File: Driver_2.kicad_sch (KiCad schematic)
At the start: 36 parts

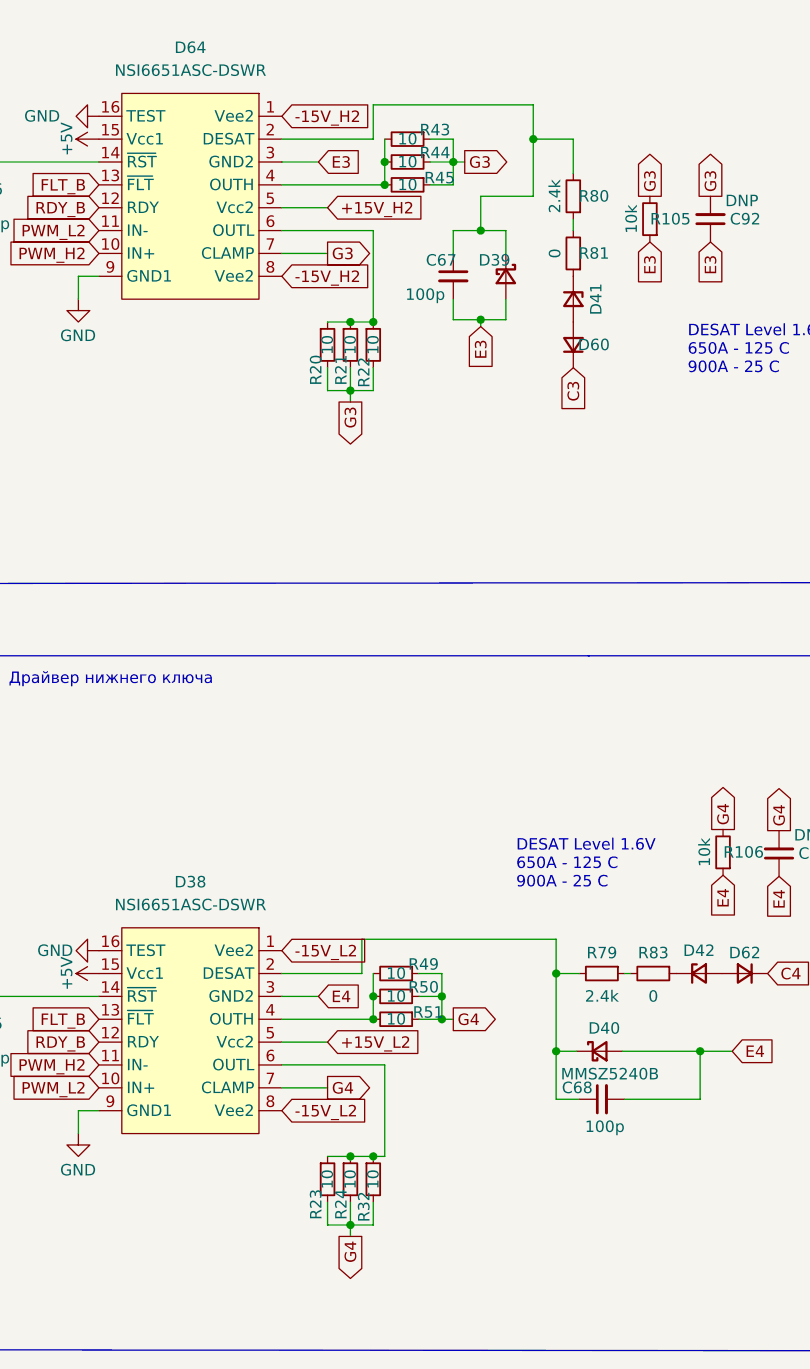
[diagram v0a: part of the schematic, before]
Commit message: VER2.2: удалил лишний затворный резистор
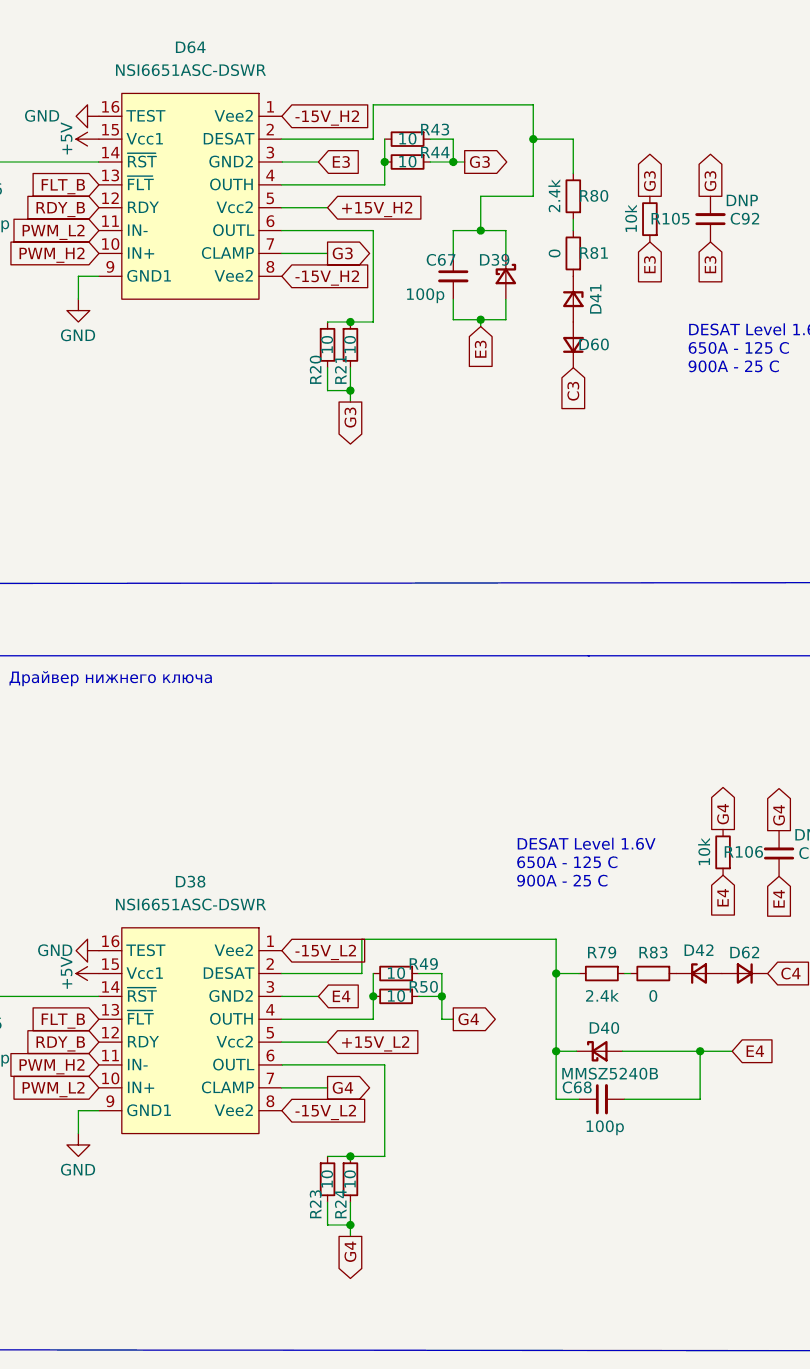
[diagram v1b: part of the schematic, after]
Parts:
- removed R22, R32, R45, R51: 10, Resistor_SMD:R_1206_3216Metric_Pad1.30x1.75mm_HandSolder, symbol Device:R_Small

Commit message: VER2.2: все изменения в списке изменений
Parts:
- D38, D64: value NSI6651ASC-DSWR -> ~; Description P/N (none) -> Gate driver; Product Name (none) -> NSI6651ASC-DSWR
- D39, D40: value MMSZ5240B -> ~; Description P/N (none) -> Zener diode; Product Name (none) -> MMSZ5240B
- D41, D42: value MMSZ5232B -> ~; Description P/N (none) -> Zener diode; Product Name (none) -> MMSZ5232B
- D60, D62: value MURS160 -> ~; Description P/N (none) -> Ultrafast diode; Product Name (none) -> MURS160

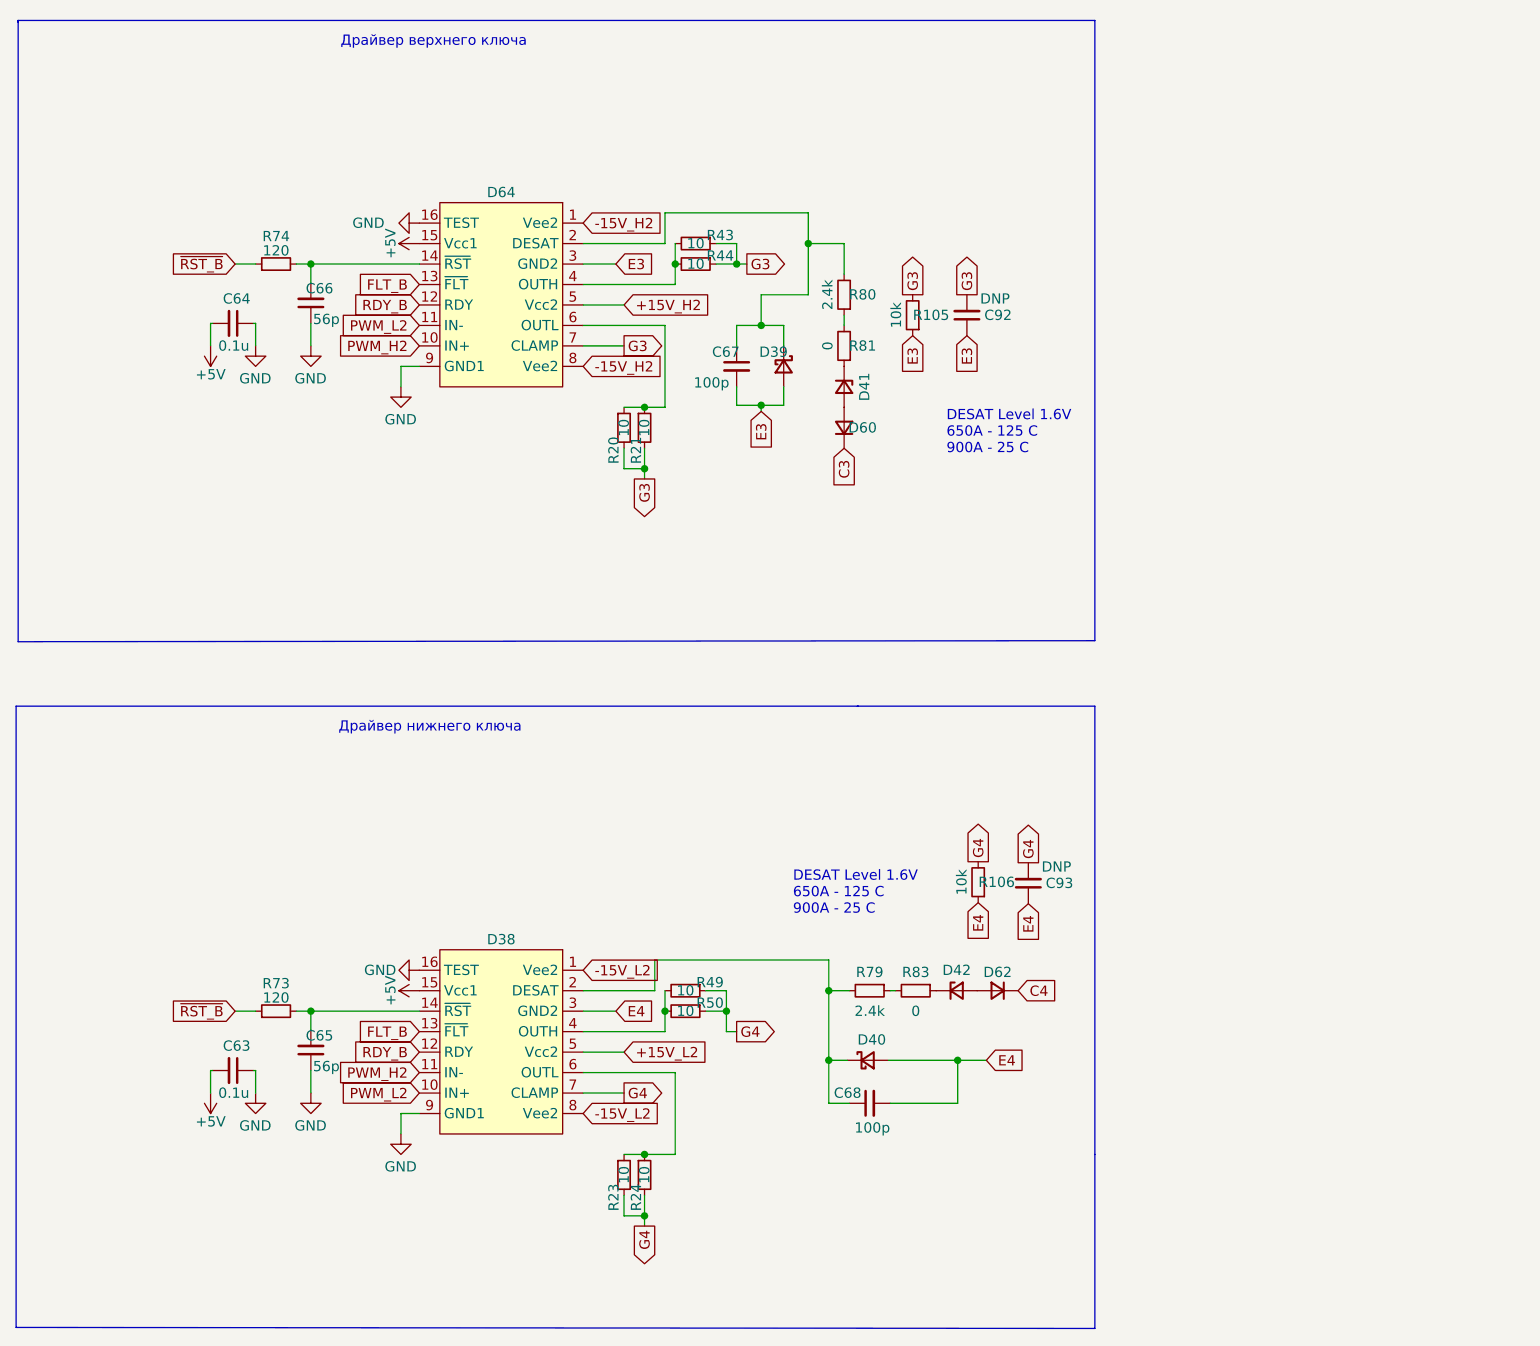
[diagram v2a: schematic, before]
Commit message: VER2.2: добавил фильтры на вход ШИМа и обновил все доки
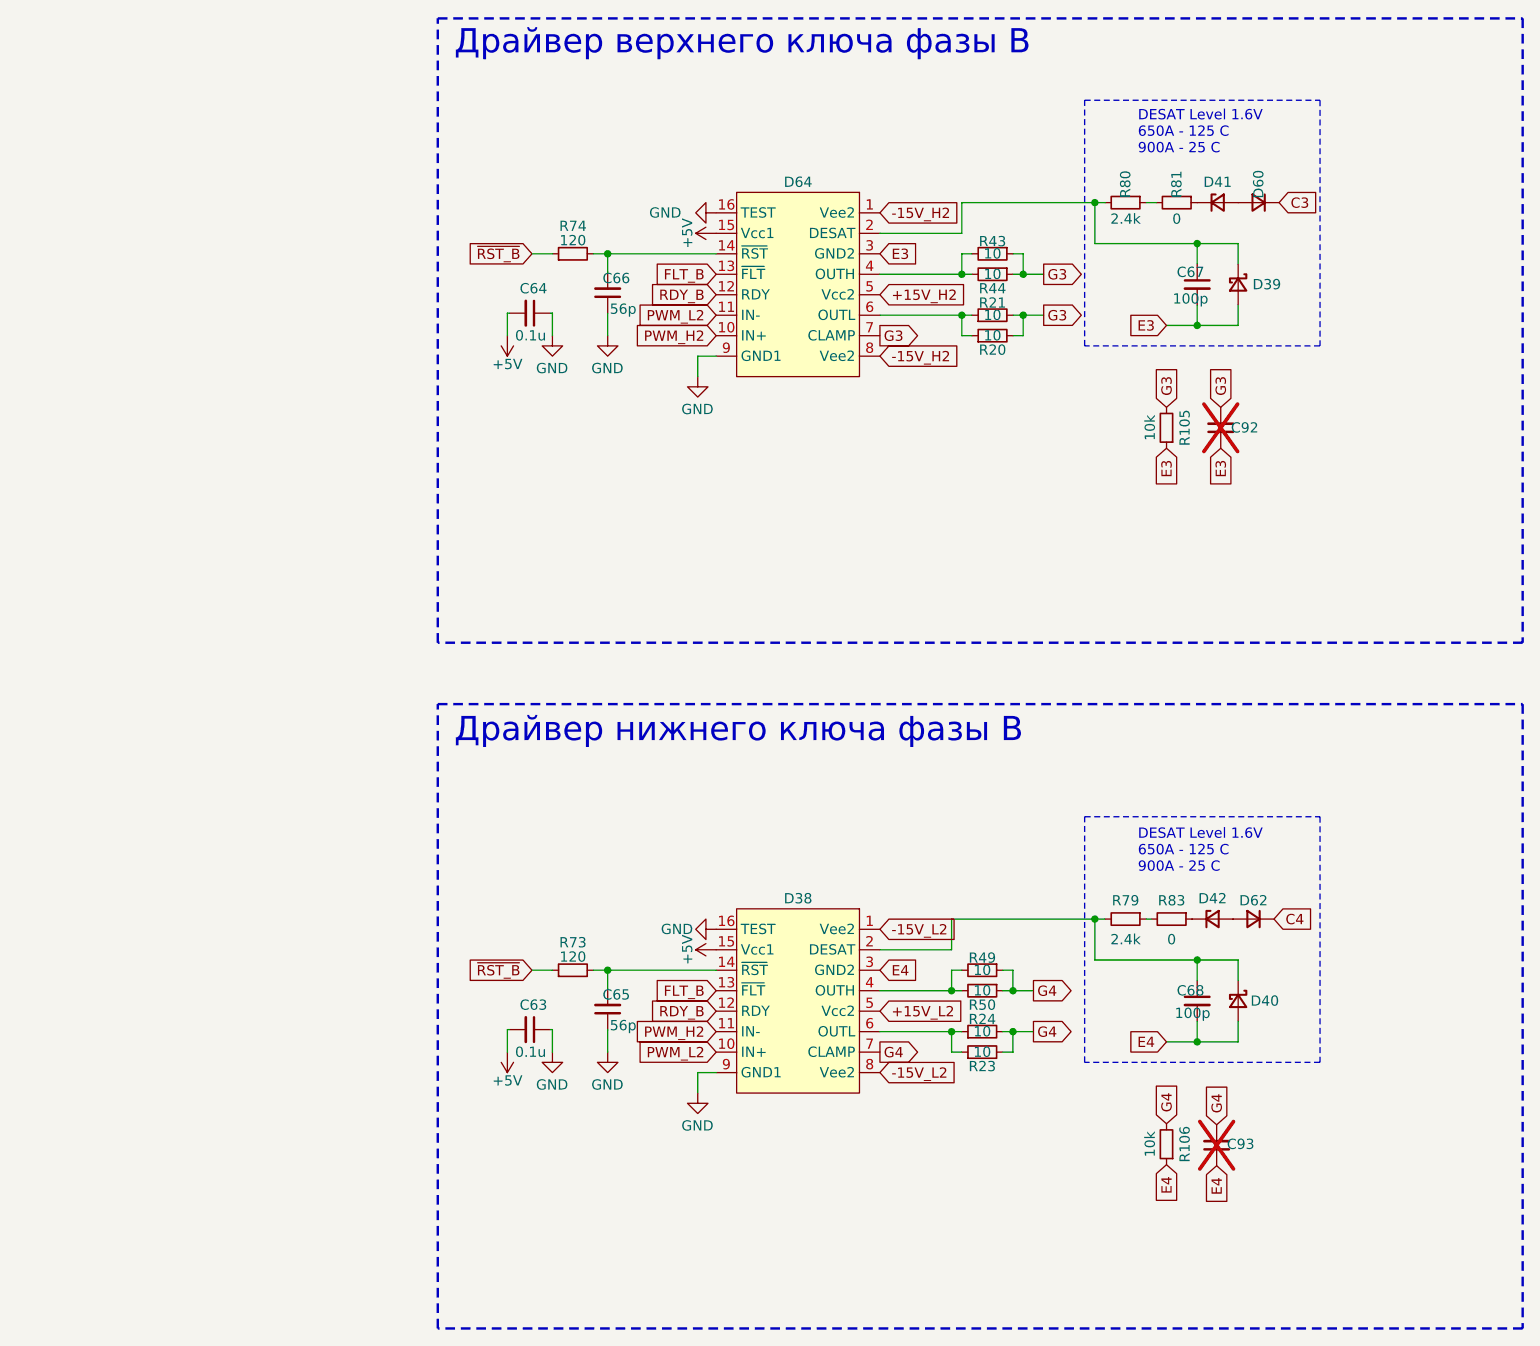
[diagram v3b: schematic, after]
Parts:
- C92, C93: value DNP -> ~; now not fitted
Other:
- note added: "Драйвер верхнего ключа фазы В"
- note added: "Драйвер нижнего ключа фазы В"
- note removed: "Драйвер верхнего ключа"
- note removed: "Драйвер нижнего ключа"
- company: (none) -> ООО "ЭТТ"
- moved on the sheet: C63, C64, C65, C66, C67, C68, D38, D39, D40, D41, D42, D60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

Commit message: VER2.2.1: исправил косяк с питанием NTC, изменил номиналы затворов и цепи NTC
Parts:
- R43, R44, R49, R50: value 10 -> 6.8
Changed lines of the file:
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@@
 			)
 		)
-		(property "Value" "10"
+		(property "Value" "6.8"
 			(at 151.13 143.51 90)
 			(effects
@@
 			)
 		)
-		(property "Value" "10"
+		(property "Value" "6.8"
 			(at 151.13 140.97 90)
 			(effects
@@
 			)
 		)
-		(property "Value" "10"
+		(property "Value" "6.8"
 			(at 152.4 52.07 90)
 			(effects
@@
 			)
 		)
-		(property "Value" "10"
+		(property "Value" "6.8"
 			(at 152.4 54.61 90)
 			(effects

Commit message: VER2.2.1: создал папку для производственных доков
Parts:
- C63, C64, C65, C66, C67, C68, C92, C93: Description P/N (none) -> Capacitor SMD 25+V
- R105, R106, R20, R21, R23, R24, R43, R44, R49, R50, R73, R74, R79, R80, R81, R83: Description P/N (none) -> Resistor SMD
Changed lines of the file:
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@@
 			)
 		)
-		(property "Description P/N" ""
+		(property "Description P/N" "Resistor SMD"
 			(at 151.13 143.51 0)
 			(effects
@@
 			)
 		)
-		(property "Description P/N" ""
+		(property "Description P/N" "Resistor SMD"
 			(at 151.13 140.97 0)
 			(effects
@@
 			)
 		)
-		(property "Description P/N" ""
+		(property "Description P/N" "Capacitor SMD 25+V"
 			(at 180.213 162.687 0)
 			(effects
@@
 			)
 		)
-		(property "Description P/N" ""
+		(property "Description P/N" "Capacitor SMD 25+V"
 			(at 104.648 145.796 0)
 			(effects
@@
 			)
 		)
-		(property "Description P/N" ""
+		(property "Description P/N" "Resistor SMD"
 			(at 152.4 59.69 0)
 			(effects
@@
 			)
 		)
-		(property "Description P/N" ""
+		(property "Description P/N" "Resistor SMD"
 			(at 173.99 73.66 0)
 			(effects
@@
 			)
 		)
-		(property "Description P/N" ""
+		(property "Description P/N" "Resistor SMD"
 			(at 152.4 62.23 0)
 			(effects
@@
 			)
 		)
-		(property "Description P/N" ""
+		(property "Description P/N" "Capacitor SMD 25+V"
 			(at 94.996 148.336 0)
 			(effects
@@
 			)
 		)
-		(property "Description P/N" ""
+		(property "Description P/N" "Capacitor SMD 25+V"
 			(at 180.721 73.66 0)
 			(effects
@@
 			)
 		)
-		(property "Description P/N" ""
+		(property "Description P/N" "Capacitor SMD 25+V"
 			(at 94.996 59.436 0)
 			(effects
@@
 			)
 		)
-		(property "Description P/N" ""
+		(property "Description P/N" "Capacitor SMD 25+V"
 			(at 177.8 144.78 0)
 			(effects
@@
 			)
 		)
-		(property "Description P/N" ""
+		(property "Description P/N" "Resistor SMD"
 			(at 151.13 151.13 0)
 			(effects
@@
 			)
 		)
-		(property "Description P/N" ""
+		(property "Description P/N" "Resistor SMD"
 			(at 152.4 52.07 0)
 			(effects
@@
 			)
 		)
-		(property "Description P/N" ""
+		(property "Description P/N" "Resistor SMD"
 			(at 100.33 140.97 0)
 			(effects
@@
 			)
 		)
-		(property "Description P/N" ""
+		(property "Description P/N" "Resistor SMD"
 			(at 173.99 162.56 0)
 			(effects
@@
 			)
 		)
-		(property "Description P/N" ""
+		(property "Description P/N" "Resistor SMD"
 			(at 100.33 52.07 0)
 			(effects
@@
 			)
 		)
-		(property "Description P/N" ""
+		(property "Description P/N" "Capacitor SMD 25+V"
 			(at 104.648 56.896 0)
 			(effects
@@
 			)
 		)
-		(property "Description P/N" ""
+		(property "Description P/N" "Resistor SMD"
 			(at 151.13 148.59 0)
 			(effects
@@
 			)
 		)
-		(property "Description P/N" ""
+		(property "Description P/N" "Resistor SMD"
 			(at 175.26 45.72 0)
 			(effects
@@
 			)
 		)
-		(property "Description P/N" ""
+		(property "Description P/N" "Resistor SMD"
 			(at 152.4 54.61 0)
 			(effects
@@
 			)
 		)
-		(property "Description P/N" ""
+		(property "Description P/N" "Resistor SMD"
 			(at 168.91 134.62 0)
 			(effects
@@
 			)
 		)
-		(property "Description P/N" ""
+		(property "Description P/N" "Resistor SMD"
 			(at 168.91 45.72 0)
 			(effects
@@
 			)
 		)
-		(property "Description P/N" ""
+		(property "Description P/N" "Resistor SMD"
 			(at 174.625 134.62 0)
 			(effects
@@
 			)
 		)
-		(property "Description P/N" ""
+		(property "Description P/N" "Capacitor SMD 25+V"
 			(at 177.8 55.88 0)
 			(effects
